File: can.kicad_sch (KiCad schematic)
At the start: 22 parts, among them Q1 2N7002K, U3 TJA1051T-3, U4 MCP2510-x/SO, U5 MAX3485CSA, Y2 16MHz

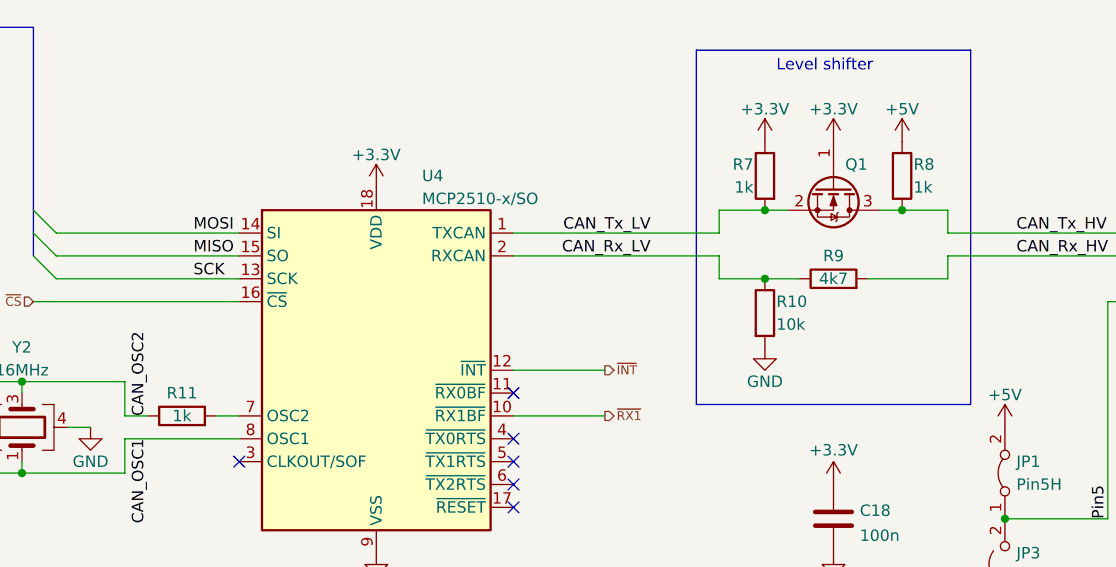
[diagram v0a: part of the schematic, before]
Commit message: rev1.1: Add I2C pullups
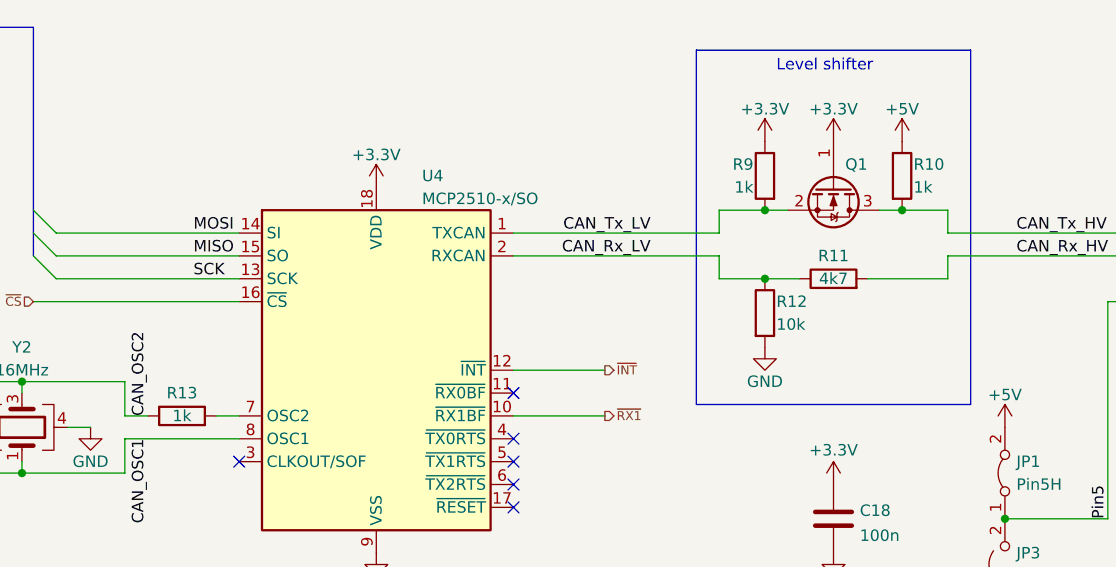
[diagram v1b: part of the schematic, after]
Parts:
- renumbered R8 to R10, R9 to R11, R10 to R12, R11 to R13, R7 to R9
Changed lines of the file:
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@@
   (title_block
     (title "[canbrd] CAN/RS485 IO board")
-    (date "2022-02-24")
-    (rev "1.0")
+    (date "2022-03-18")
+    (rev "1.1")
   )
   (junction (at 144.78 78.74) (diameter 0) (color 0 0 0 0)
@@
   (symbol (lib_id "power:+3.3V") (at 152.4 154.94 0) (unit 1)
     (in_bom yes) (on_board yes)
-    (property "Reference" "#PWR049" (id 0) (at 152.4 158.75 0)
+    (property "Reference" "#PWR051" (id 0) (at 152.4 158.75 0)
       (effects (font (size 1.27 1.27)) hide)
     )
@@
   (symbol (lib_id "power:GND") (at 101.6 153.67 0) (unit 1)
     (in_bom yes) (on_board yes)
-    (property "Reference" "#PWR048" (id 0) (at 101.6 160.02 0)
+    (property "Reference" "#PWR050" (id 0) (at 101.6 160.02 0)
       (effects (font (size 1.27 1.27)) hide)
     )
@@
   (symbol (lib_id "power:GND") (at 241.3 93.98 0) (unit 1)
     (in_bom yes) (on_board yes)
-    (property "Reference" "#PWR035" (id 0) (at 241.3 100.33 0)
+    (property "Reference" "#PWR037" (id 0) (at 241.3 100.33 0)
       (effects (font (size 1.27 1.27)) hide)
     )
@@
   (symbol (lib_id "power:GND") (at 144.78 86.36 0) (unit 1)
     (in_bom yes) (on_board yes)
-    (property "Reference" "#PWR033" (id 0) (at 144.78 92.71 0)
+    (property "Reference" "#PWR035" (id 0) (at 144.78 92.71 0)
       (effects (font (size 1.27 1.27)) hide)
     )
@@
   (symbol (lib_id "power:+5V") (at 190.5 95.25 0) (unit 1)
     (in_bom yes) (on_board yes)
-    (property "Reference" "#PWR038" (id 0) (at 190.5 99.06 0)
+    (property "Reference" "#PWR040" (id 0) (at 190.5 99.06 0)
       (effects (font (size 1.27 1.27)) hide)
     )
@@
   (symbol (lib_id "power:+5V") (at 203.2 68.58 0) (unit 1)
     (in_bom yes) (on_board yes) (fields_autoplaced)
-    (property "Reference" "#PWR032" (id 0) (at 203.2 72.39 0)
+    (property "Reference" "#PWR034" (id 0) (at 203.2 72.39 0)
       (effects (font (size 1.27 1.27)) hide)
     )
@@
   (symbol (lib_id "power:+3.3V") (at 152.4 101.6 0) (unit 1)
     (in_bom yes) (on_board yes)
-    (property "Reference" "#PWR039" (id 0) (at 152.4 105.41 0)
+    (property "Reference" "#PWR041" (id 0) (at 152.4 105.41 0)
       (effects (font (size 1.27 1.27)) hide)
     )
@@
   (symbol (lib_id "power:+5V") (at 160.02 63.5 0) (unit 1)
     (in_bom yes) (on_board yes) (fields_autoplaced)
-    (property "Reference" "#PWR030" (id 0) (at 160.02 67.31 0)
+    (property "Reference" "#PWR032" (id 0) (at 160.02 67.31 0)
       (effects (font (size 1.27 1.27)) hide)
     )
@@
   (symbol (lib_id "Device:R") (at 160.02 67.31 0) (unit 1)
     (in_bom yes) (on_board yes)
-    (property "Reference" "R8" (id 0) (at 161.29 66.04 0)
+    (property "Reference" "R10" (id 0) (at 161.29 66.04 0)
       (effects (font (size 1.27 1.27)) (justify left))
     )
@@
   (symbol (lib_id "power:+5V") (at 171.45 95.25 0) (unit 1)
     (in_bom yes) (on_board yes) (fields_autoplaced)
-    (property "Reference" "#PWR037" (id 0) (at 171.45 99.06 0)
+    (property "Reference" "#PWR039" (id 0) (at 171.45 99.06 0)
       (effects (font (size 1.27 1.27)) hide)
     )
@@
   (symbol (lib_id "Device:R") (at 152.4 78.74 90) (unit 1)
     (in_bom yes) (on_board yes)
-    (property "Reference" "R9" (id 0) (at 152.4 76.2 90))
+    (property "Reference" "R11" (id 0) (at 152.4 76.2 90))
     (property "Value" "4k7" (id 1) (at 152.4 78.74 90))
     (property "Footprint" "Resistor_SMD:R_0603_1608Metric" (id 2) (at 152.4 80.518 90)
@@
   (symbol (lib_id "power:GND") (at 43.18 102.87 0) (unit 1)
     (in_bom yes) (on_board yes)
-    (property "Reference" "#PWR041" (id 0) (at 43.18 109.22 0)
+    (property "Reference" "#PWR043" (id 0) (at 43.18 109.22 0)
       (effects (font (size 1.27 1.27)) hide)
     )
@@
   (symbol (lib_id "power:+3.3V") (at 152.4 63.5 0) (unit 1)
     (in_bom yes) (on_board yes)
-    (property "Reference" "#PWR029" (id 0) (at 152.4 67.31 0)
+    (property "Reference" "#PWR031" (id 0) (at 152.4 67.31 0)
       (effects (font (size 1.27 1.27)) hide)
     )
@@
   (symbol (lib_id "Device:R") (at 144.78 67.31 0) (mirror y) (unit 1)
     (in_bom yes) (on_board yes)
-    (property "Reference" "R7" (id 0) (at 143.51 66.04 0)
+    (property "Reference" "R9" (id 0) (at 143.51 66.04 0)
       (effects (font (size 1.27 1.27)) (justify left))
     )
@@
   (symbol (lib_id "power:GND") (at 152.4 162.56 0) (unit 1)
     (in_bom yes) (on_board yes)
-    (property "Reference" "#PWR050" (id 0) (at 152.4 168.91 0)
+    (property "Reference" "#PWR052" (id 0) (at 152.4 168.91 0)
       (effects (font (size 1.27 1.27)) hide)
     )
@@
   (symbol (lib_id "power:+5V") (at 203.2 101.6 0) (unit 1)
     (in_bom yes) (on_board yes)
-    (property "Reference" "#PWR040" (id 0) (at 203.2 105.41 0)
+    (property "Reference" "#PWR042" (id 0) (at 203.2 105.41 0)
       (effects (font (size 1.27 1.27)) hide)
     )
@@
   (symbol (lib_id "power:+3.3V") (at 144.78 63.5 0) (unit 1)
     (in_bom yes) (on_board yes) (fields_autoplaced)
-    (property "Reference" "#PWR028" (id 0) (at 144.78 67.31 0)
+    (property "Reference" "#PWR030" (id 0) (at 144.78 67.31 0)
       (effects (font (size 1.27 1.27)) hide)
     )
@@
   (symbol (lib_id "power:+3.3V") (at 101.6 125.73 0) (unit 1)
     (in_bom yes) (on_board yes)
-    (property "Reference" "#PWR047" (id 0) (at 101.6 129.54 0)
+    (property "Reference" "#PWR049" (id 0) (at 101.6 129.54 0)
       (effects (font (size 1.27 1.27)) hide)
     )
@@
   (symbol (lib_id "power:GND") (at 69.85 95.25 0) (unit 1)
     (in_bom yes) (on_board yes)
-    (property "Reference" "#PWR036" (id 0) (at 69.85 101.6 0)
+    (property "Reference" "#PWR038" (id 0) (at 69.85 101.6 0)
       (effects (font (size 1.27 1.27)) hide)
     )
@@
   (symbol (lib_id "power:GND") (at 171.45 115.57 0) (unit 1)
     (in_bom yes) (on_board yes)
-    (property "Reference" "#PWR045" (id 0) (at 171.45 121.92 0)
+    (property "Reference" "#PWR047" (id 0) (at 171.45 121.92 0)
       (effects (font (size 1.27 1.27)) hide)
     )
@@
   (symbol (lib_id "power:GND") (at 152.4 109.22 0) (unit 1)
     (in_bom yes) (on_board yes)
-    (property "Reference" "#PWR043" (id 0) (at 152.4 115.57 0)
+    (property "Reference" "#PWR045" (id 0) (at 152.4 115.57 0)
       (effects (font (size 1.27 1.27)) hide)
     )
@@
   (symbol (lib_id "Device:R") (at 144.78 82.55 0) (unit 1)
     (in_bom yes) (on_board yes)
-    (property "Reference" "R10" (id 0) (at 146.05 81.28 0)
+    (property "Reference" "R12" (id 0) (at 146.05 81.28 0)
       (effects (font (size 1.27 1.27)) (justify left))
     )
@@
   (symbol (lib_id "Device:R") (at 80.01 93.98 90) (unit 1)
     (in_bom yes) (on_board yes)
-    (property "Reference" "R11" (id 0) (at 80.01 91.44 90))
+    (property "Reference" "R13" (id 0) (at 80.01 91.44 90))
     (property "Value" "1k" (id 1) (at 80.01 93.98 90))
     (property "Footprint" "Resistor_SMD:R_0603_1608Metric" (id 2) (at 80.01 95.758 90)
@@
   (symbol (lib_id "power:GND") (at 190.5 115.57 0) (unit 1)
     (in_bom yes) (on_board yes)
-    (property "Reference" "#PWR046" (id 0) (at 190.5 121.92 0)
+    (property "Reference" "#PWR048" (id 0) (at 190.5 121.92 0)
       (effects (font (size 1.27 1.27)) hide)
     )
@@
   (symbol (lib_id "power:GND") (at 101.6 109.22 0) (unit 1)
     (in_bom yes) (on_board yes)
-    (property "Reference" "#PWR042" (id 0) (at 101.6 115.57 0)
+    (property "Reference" "#PWR044" (id 0) (at 101.6 115.57 0)
       (effects (font (size 1.27 1.27)) hide)
     )
@@
   (symbol (lib_id "power:+3.3V") (at 101.6 68.58 0) (unit 1)
     (in_bom yes) (on_board yes) (fields_autoplaced)
-    (property "Reference" "#PWR031" (id 0) (at 101.6 72.39 0)
+    (property "Reference" "#PWR033" (id 0) (at 101.6 72.39 0)
       (effects (font (size 1.27 1.27)) hide)
     )
@@
   (symbol (lib_id "power:GND") (at 203.2 88.9 0) (unit 1)
     (in_bom yes) (on_board yes)
-    (property "Reference" "#PWR034" (id 0) (at 203.2 95.25 0)
+    (property "Reference" "#PWR036" (id 0) (at 203.2 95.25 0)
       (effects (font (size 1.27 1.27)) hide)
     )
@@
   (symbol (lib_id "power:GND") (at 203.2 109.22 0) (unit 1)
     (in_bom yes) (on_board yes)
-    (property "Reference" "#PWR044" (id 0) (at 203.2 115.57 0)
-      (effects (font (size 1.27 1.27)) hide)
-    )
+    (property "Reference" "#PWR046" (id 0) (at 203.2 115.57 0)
+      (effects (font (size 1.27 1.27)) hide)
+    )

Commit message: lots changed
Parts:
- renumbered R12 to R10, R13 to R11, R9 to R7, R10 to R8, R11 to R9
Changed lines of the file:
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@@
   (title_block
     (title "[canbrd] CAN/RS485 IO board")
-    (date "2022-03-18")
-    (rev "1.1")
+    (date "2022-04-03")
+    (rev "2.0")
   )
   (junction (at 144.78 78.74) (diameter 0) (color 0 0 0 0)
@@
   (symbol (lib_id "power:+3.3V") (at 152.4 154.94 0) (unit 1)
     (in_bom yes) (on_board yes)
-    (property "Reference" "#PWR051" (id 0) (at 152.4 158.75 0)
+    (property "Reference" "#PWR049" (id 0) (at 152.4 158.75 0)
       (effects (font (size 1.27 1.27)) hide)
     )
@@
   (symbol (lib_id "power:GND") (at 101.6 153.67 0) (unit 1)
     (in_bom yes) (on_board yes)
-    (property "Reference" "#PWR050" (id 0) (at 101.6 160.02 0)
+    (property "Reference" "#PWR048" (id 0) (at 101.6 160.02 0)
       (effects (font (size 1.27 1.27)) hide)
     )
@@
   (symbol (lib_id "power:GND") (at 241.3 93.98 0) (unit 1)
     (in_bom yes) (on_board yes)
-    (property "Reference" "#PWR037" (id 0) (at 241.3 100.33 0)
+    (property "Reference" "#PWR035" (id 0) (at 241.3 100.33 0)
       (effects (font (size 1.27 1.27)) hide)
     )
@@
   (symbol (lib_id "power:GND") (at 144.78 86.36 0) (unit 1)
     (in_bom yes) (on_board yes)
-    (property "Reference" "#PWR035" (id 0) (at 144.78 92.71 0)
+    (property "Reference" "#PWR033" (id 0) (at 144.78 92.71 0)
       (effects (font (size 1.27 1.27)) hide)
     )
@@
   (symbol (lib_id "power:+5V") (at 190.5 95.25 0) (unit 1)
     (in_bom yes) (on_board yes)
-    (property "Reference" "#PWR040" (id 0) (at 190.5 99.06 0)
+    (property "Reference" "#PWR038" (id 0) (at 190.5 99.06 0)
       (effects (font (size 1.27 1.27)) hide)
     )
@@
   (symbol (lib_id "power:+5V") (at 203.2 68.58 0) (unit 1)
     (in_bom yes) (on_board yes) (fields_autoplaced)
-    (property "Reference" "#PWR034" (id 0) (at 203.2 72.39 0)
+    (property "Reference" "#PWR032" (id 0) (at 203.2 72.39 0)
       (effects (font (size 1.27 1.27)) hide)
     )
@@
   (symbol (lib_id "power:+3.3V") (at 152.4 101.6 0) (unit 1)
     (in_bom yes) (on_board yes)
-    (property "Reference" "#PWR041" (id 0) (at 152.4 105.41 0)
+    (property "Reference" "#PWR039" (id 0) (at 152.4 105.41 0)
       (effects (font (size 1.27 1.27)) hide)
     )
@@
   (symbol (lib_id "power:+5V") (at 160.02 63.5 0) (unit 1)
     (in_bom yes) (on_board yes) (fields_autoplaced)
-    (property "Reference" "#PWR032" (id 0) (at 160.02 67.31 0)
+    (property "Reference" "#PWR030" (id 0) (at 160.02 67.31 0)
       (effects (font (size 1.27 1.27)) hide)
     )
@@
   (symbol (lib_id "Device:R") (at 160.02 67.31 0) (unit 1)
     (in_bom yes) (on_board yes)
-    (property "Reference" "R10" (id 0) (at 161.29 66.04 0)
+    (property "Reference" "R8" (id 0) (at 161.29 66.04 0)
       (effects (font (size 1.27 1.27)) (justify left))
     )
@@
   (symbol (lib_id "power:+5V") (at 171.45 95.25 0) (unit 1)
     (in_bom yes) (on_board yes) (fields_autoplaced)
-    (property "Reference" "#PWR039" (id 0) (at 171.45 99.06 0)
+    (property "Reference" "#PWR037" (id 0) (at 171.45 99.06 0)
       (effects (font (size 1.27 1.27)) hide)
     )
@@
   (symbol (lib_id "Device:R") (at 152.4 78.74 90) (unit 1)
     (in_bom yes) (on_board yes)
-    (property "Reference" "R11" (id 0) (at 152.4 76.2 90))
+    (property "Reference" "R9" (id 0) (at 152.4 76.2 90))
     (property "Value" "4k7" (id 1) (at 152.4 78.74 90))
     (property "Footprint" "Resistor_SMD:R_0603_1608Metric" (id 2) (at 152.4 80.518 90)
@@
   (symbol (lib_id "power:GND") (at 43.18 102.87 0) (unit 1)
     (in_bom yes) (on_board yes)
-    (property "Reference" "#PWR043" (id 0) (at 43.18 109.22 0)
+    (property "Reference" "#PWR041" (id 0) (at 43.18 109.22 0)
       (effects (font (size 1.27 1.27)) hide)
     )
@@
   (symbol (lib_id "power:+3.3V") (at 152.4 63.5 0) (unit 1)
     (in_bom yes) (on_board yes)
-    (property "Reference" "#PWR031" (id 0) (at 152.4 67.31 0)
+    (property "Reference" "#PWR029" (id 0) (at 152.4 67.31 0)
       (effects (font (size 1.27 1.27)) hide)
     )
@@
   (symbol (lib_id "Device:R") (at 144.78 67.31 0) (mirror y) (unit 1)
     (in_bom yes) (on_board yes)
-    (property "Reference" "R9" (id 0) (at 143.51 66.04 0)
+    (property "Reference" "R7" (id 0) (at 143.51 66.04 0)
       (effects (font (size 1.27 1.27)) (justify left))
     )
@@
   (symbol (lib_id "power:GND") (at 152.4 162.56 0) (unit 1)
     (in_bom yes) (on_board yes)
-    (property "Reference" "#PWR052" (id 0) (at 152.4 168.91 0)
+    (property "Reference" "#PWR050" (id 0) (at 152.4 168.91 0)
       (effects (font (size 1.27 1.27)) hide)
     )
@@
   (symbol (lib_id "power:+5V") (at 203.2 101.6 0) (unit 1)
     (in_bom yes) (on_board yes)
-    (property "Reference" "#PWR042" (id 0) (at 203.2 105.41 0)
+    (property "Reference" "#PWR040" (id 0) (at 203.2 105.41 0)
       (effects (font (size 1.27 1.27)) hide)
     )
@@
   (symbol (lib_id "power:+3.3V") (at 144.78 63.5 0) (unit 1)
     (in_bom yes) (on_board yes) (fields_autoplaced)
-    (property "Reference" "#PWR030" (id 0) (at 144.78 67.31 0)
+    (property "Reference" "#PWR028" (id 0) (at 144.78 67.31 0)
       (effects (font (size 1.27 1.27)) hide)
     )
@@
   (symbol (lib_id "power:+3.3V") (at 101.6 125.73 0) (unit 1)
     (in_bom yes) (on_board yes)
-    (property "Reference" "#PWR049" (id 0) (at 101.6 129.54 0)
+    (property "Reference" "#PWR047" (id 0) (at 101.6 129.54 0)
       (effects (font (size 1.27 1.27)) hide)
     )
@@
   (symbol (lib_id "power:GND") (at 69.85 95.25 0) (unit 1)
     (in_bom yes) (on_board yes)
-    (property "Reference" "#PWR038" (id 0) (at 69.85 101.6 0)
+    (property "Reference" "#PWR036" (id 0) (at 69.85 101.6 0)
       (effects (font (size 1.27 1.27)) hide)
     )
@@
   (symbol (lib_id "power:GND") (at 171.45 115.57 0) (unit 1)
     (in_bom yes) (on_board yes)
-    (property "Reference" "#PWR047" (id 0) (at 171.45 121.92 0)
+    (property "Reference" "#PWR045" (id 0) (at 171.45 121.92 0)
       (effects (font (size 1.27 1.27)) hide)
     )
@@
   (symbol (lib_id "power:GND") (at 152.4 109.22 0) (unit 1)
     (in_bom yes) (on_board yes)
-    (property "Reference" "#PWR045" (id 0) (at 152.4 115.57 0)
+    (property "Reference" "#PWR043" (id 0) (at 152.4 115.57 0)
       (effects (font (size 1.27 1.27)) hide)
     )
@@
   (symbol (lib_id "Device:R") (at 144.78 82.55 0) (unit 1)
     (in_bom yes) (on_board yes)
-    (property "Reference" "R12" (id 0) (at 146.05 81.28 0)
+    (property "Reference" "R10" (id 0) (at 146.05 81.28 0)
       (effects (font (size 1.27 1.27)) (justify left))
     )
@@
   (symbol (lib_id "Device:R") (at 80.01 93.98 90) (unit 1)
     (in_bom yes) (on_board yes)
-    (property "Reference" "R13" (id 0) (at 80.01 91.44 90))
+    (property "Reference" "R11" (id 0) (at 80.01 91.44 90))
     (property "Value" "1k" (id 1) (at 80.01 93.98 90))
     (property "Footprint" "Resistor_SMD:R_0603_1608Metric" (id 2) (at 80.01 95.758 90)
@@
   (symbol (lib_id "power:GND") (at 190.5 115.57 0) (unit 1)
     (in_bom yes) (on_board yes)
-    (property "Reference" "#PWR048" (id 0) (at 190.5 121.92 0)
+    (property "Reference" "#PWR046" (id 0) (at 190.5 121.92 0)
       (effects (font (size 1.27 1.27)) hide)
     )
@@
   (symbol (lib_id "power:GND") (at 101.6 109.22 0) (unit 1)
     (in_bom yes) (on_board yes)
-    (property "Reference" "#PWR044" (id 0) (at 101.6 115.57 0)
+    (property "Reference" "#PWR042" (id 0) (at 101.6 115.57 0)
       (effects (font (size 1.27 1.27)) hide)
     )
@@
   (symbol (lib_id "power:+3.3V") (at 101.6 68.58 0) (unit 1)
     (in_bom yes) (on_board yes) (fields_autoplaced)
-    (property "Reference" "#PWR033" (id 0) (at 101.6 72.39 0)
+    (property "Reference" "#PWR031" (id 0) (at 101.6 72.39 0)
       (effects (font (size 1.27 1.27)) hide)
     )
@@
   (symbol (lib_id "power:GND") (at 203.2 88.9 0) (unit 1)
     (in_bom yes) (on_board yes)
-    (property "Reference" "#PWR036" (id 0) (at 203.2 95.25 0)
+    (property "Reference" "#PWR034" (id 0) (at 203.2 95.25 0)
       (effects (font (size 1.27 1.27)) hide)
     )
@@
   (symbol (lib_id "power:GND") (at 203.2 109.22 0) (unit 1)
     (in_bom yes) (on_board yes)
-    (property "Reference" "#PWR046" (id 0) (at 203.2 115.57 0)
-      (effects (font (size 1.27 1.27)) hide)
-    )
+    (property "Reference" "#PWR044" (id 0) (at 203.2 115.57 0)
+      (effects (font (size 1.27 1.27)) hide)
+    )

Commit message: things changed
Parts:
- removed D3: NUP2105L, Package_TO_SOT_SMD:SOT-23, symbol Power_Protection:NUP2105L
- removed Q1: 2N7002K, Package_TO_SOT_SMD:SOT-23, symbol Transistor_FET:2N7002K
- removed R7, R8: 1k, Resistor_SMD:R_0603_1608Metric, symbol Device:R
- removed R9: 4k7, Resistor_SMD:R_0603_1608Metric, symbol Device:R
- added C20, C21, C22: 47p, Capacitor_SMD:C_0603_1608Metric, symbol Device:C_Small
- added D2: NUP2105L, Package_TO_SOT_SMD:SOT-23, symbol Power_Protection:NUP2105L
- added R12: DNP, Resistor_SMD:R_0603_1608Metric, symbol Device:R_Small
- D1: MANUFACTURER Bourns -> (none)
- D3: renamed from D2; MANUFACTURER Bourns -> (none)
- R10: value 10k -> 130
- renumbered C16 to C23, C17 to C24, C20 to C25
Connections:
- net +5V: no longer C19.1, JP1.2 (B), JP2.1 (A), U3.3 (VCC)
- net GND: no longer C19.2, JP3.1 (A), JP4.2 (B), R10.2, U3.2 (GND)
- net MISO: now also R10.1; no longer U4.15 (SO)
- net at D3.1, U3.6 (CANL), U5.7 (B): now also C21.2, C22.2, D2.1 (K)
- net at D1.1, U3.7 (CANH), U5.6 (A): now also C20.1, C21.1, D2.2 (K)
- net CAN_OSC1 renamed OSC1
- net OSC1: now also R12.2
- net CAN_OSC2 renamed OSC2
- net OSC2: now also R12.1
- net CAN_Rx_HV renamed CAN_Rx_ISO
- net CAN_Rx_LV renamed CAN_Rx
- net CAN_Rx: no longer R10.1
- net CAN_Tx_HV renamed CAN_Tx_ISO
- net CAN_Tx_LV renamed CAN_Tx
- new net +5VISO: C19.1, JP1.2 (B), JP2.1 (A), U3.3 (VCC)
- new net GNDISO: C19.2, C20.2, C22.1, D2.3 (A), JP3.1 (A), JP4.2 (B), U3.2 (GND)
- new net xMISO: R10.2, U4.15 (SO)
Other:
- added sheet CAN Isolation (isolation.kicad_sch)
- note added: "RS485 is not isolated!"
- note removed: "Level shifter"
- moved on the sheet: C18, C19, C23, C24, C25, D1, D3, JP1, JP2, JP3, JP4, R11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

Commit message: isolate and other stuff
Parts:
- removed C25: 100n, Capacitor_SMD:C_0603_1608Metric, symbol Device:C
- removed U5: MAX3485CSA, Package_SO:SOIC-8_3.9x4.9mm_P1.27mm, symbol Interface_UART:MAX3485
- C23, C24: value ??? -> 10p
- R10: value 130 -> 100
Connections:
- net +3V3: now also U4.17 (~{RESET})
- no-connect marks 6 -> 5
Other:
- sheet CAN Isolation ports: added 3.3V; removed none
- note removed: "RS485 is not isolated!"
- title: [canbrd] CAN/RS485 IO board -> [canbrd] CAN IO board
- moved on the sheet: C18, C19, C20, C21, C22, C23, C24, D1, D2, D3, JP1, JP2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

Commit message: things changed
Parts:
- renumbered C18 to C31, C19 to C32, C20 to C33, C21 to C34, C22 to C35, C23 to C36, C24 to C37, D1 to D22, D2 to D23, D3 to D24, JP1 to JP3, JP2 to JP4, JP3 to JP5, JP4 to JP6, R10 to R48, R11 to R49, R12 to R50, U3 to U7, U4 to U8
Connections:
- net +3V3 renamed +3.3V
- net ~{RX1}: no longer names the net of U8.10 (~{RX1BF})
- no-connect marks 5 -> 6
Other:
- moved on the sheet: C36, C37, R50, Y2
